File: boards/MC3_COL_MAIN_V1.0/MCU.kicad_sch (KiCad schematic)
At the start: 17 parts, among them J2 SWD, SW1 SKRKAEE020, U2 STM32F411RET6, Y1 8MHz

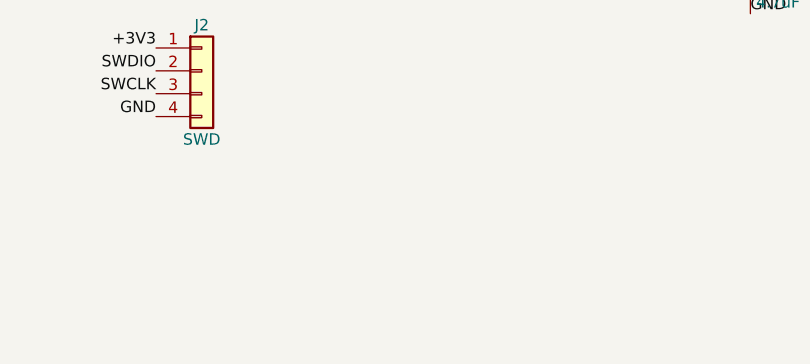
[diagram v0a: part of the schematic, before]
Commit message: Schematic: I2C1 pull-ups (R12/R13 4.7k, PROVISIONAL); DRV8214 layout note; parts README and MIGRATION updated
Co-Authored-By: Claude Fable 5 <noreply@anthropic.com>
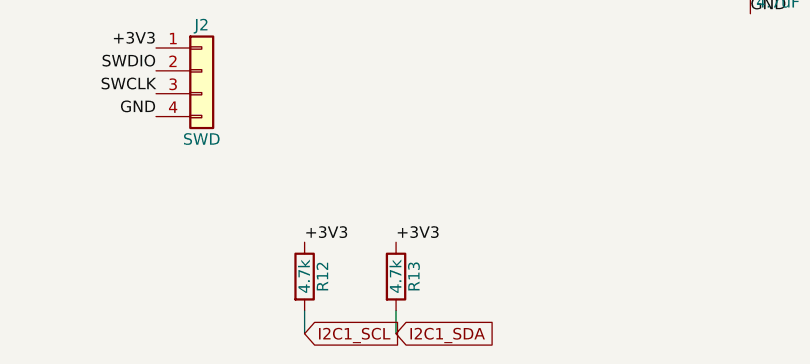
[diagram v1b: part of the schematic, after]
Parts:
- added R12, R13: 4.7k, MC3_COL_MAIN:R_0402_1005Metric, symbol Device:R
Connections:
- net +3V3: now also R12.1, R13.1
- net I2C1_SCL: now also R12.2
- net I2C1_SDA: now also R13.2

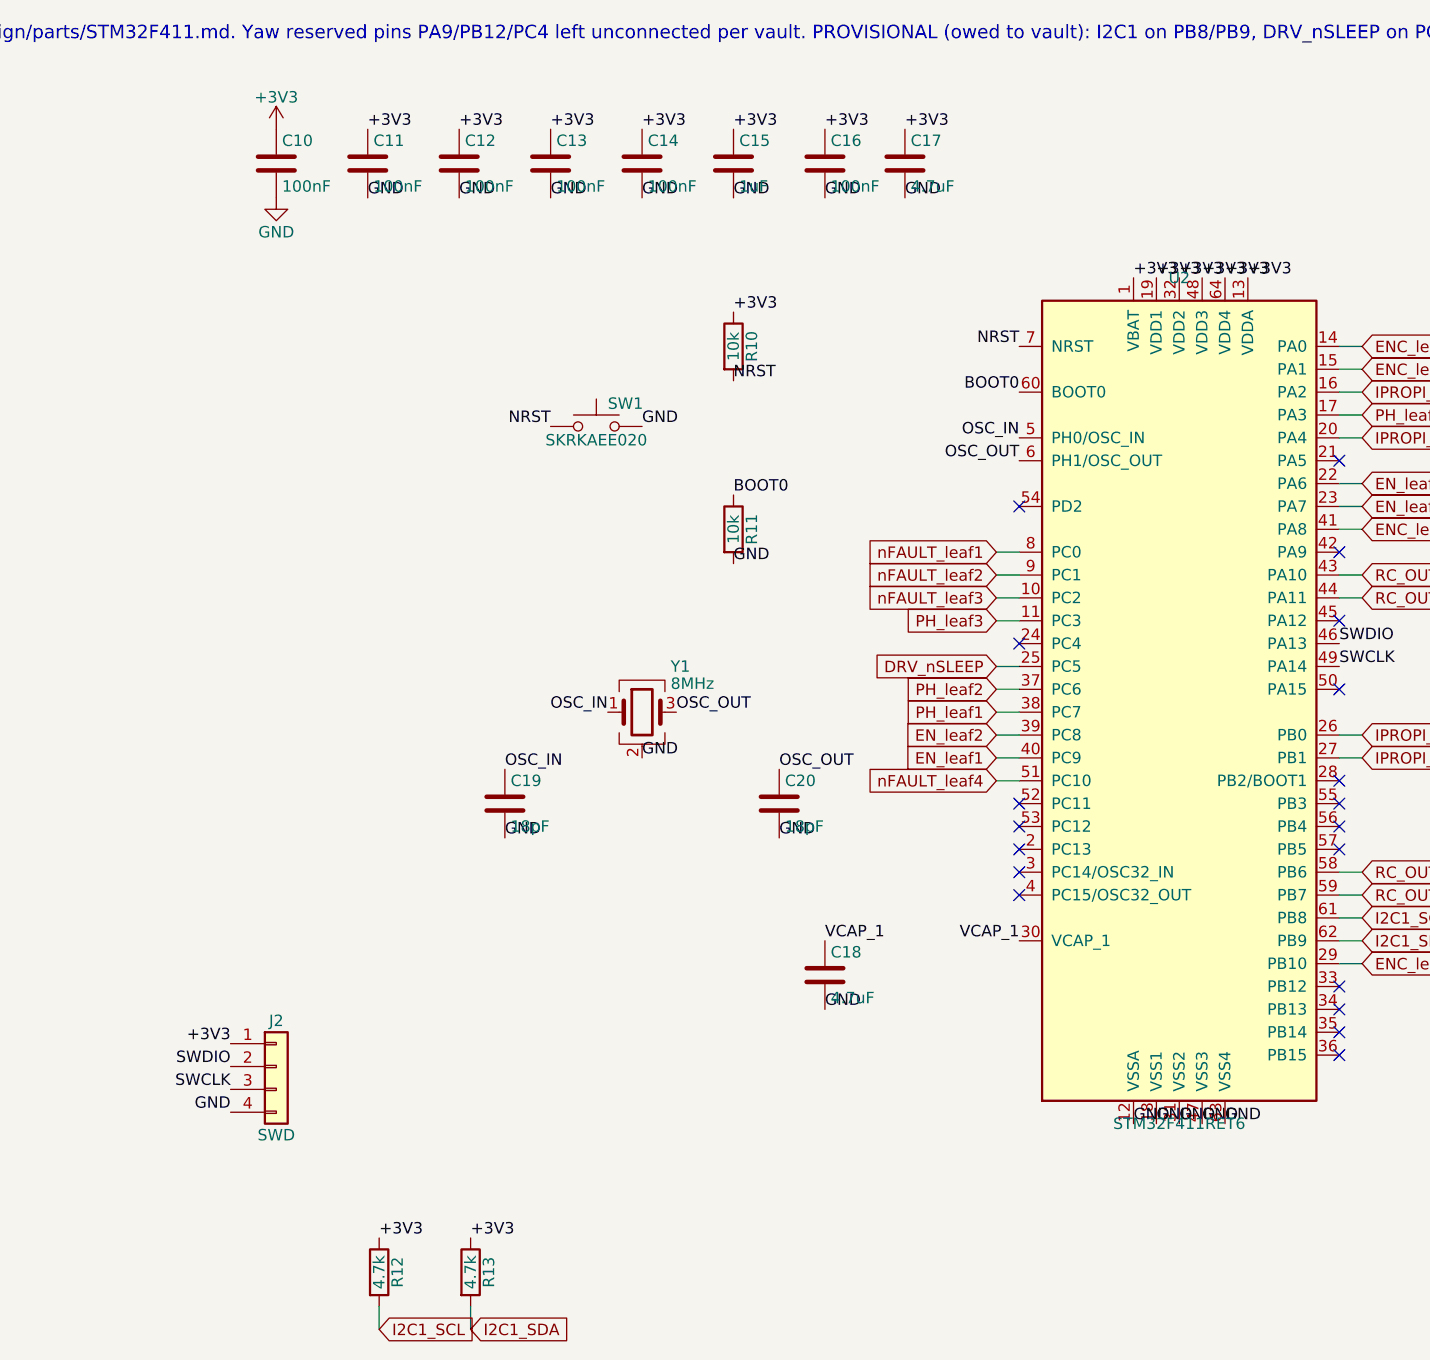
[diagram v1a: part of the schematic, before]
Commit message: Schematic annotated in eeschema (per-instance references for the 4 channel sheets); user review OK
Co-Authored-By: Claude Fable 5 <noreply@anthropic.com>
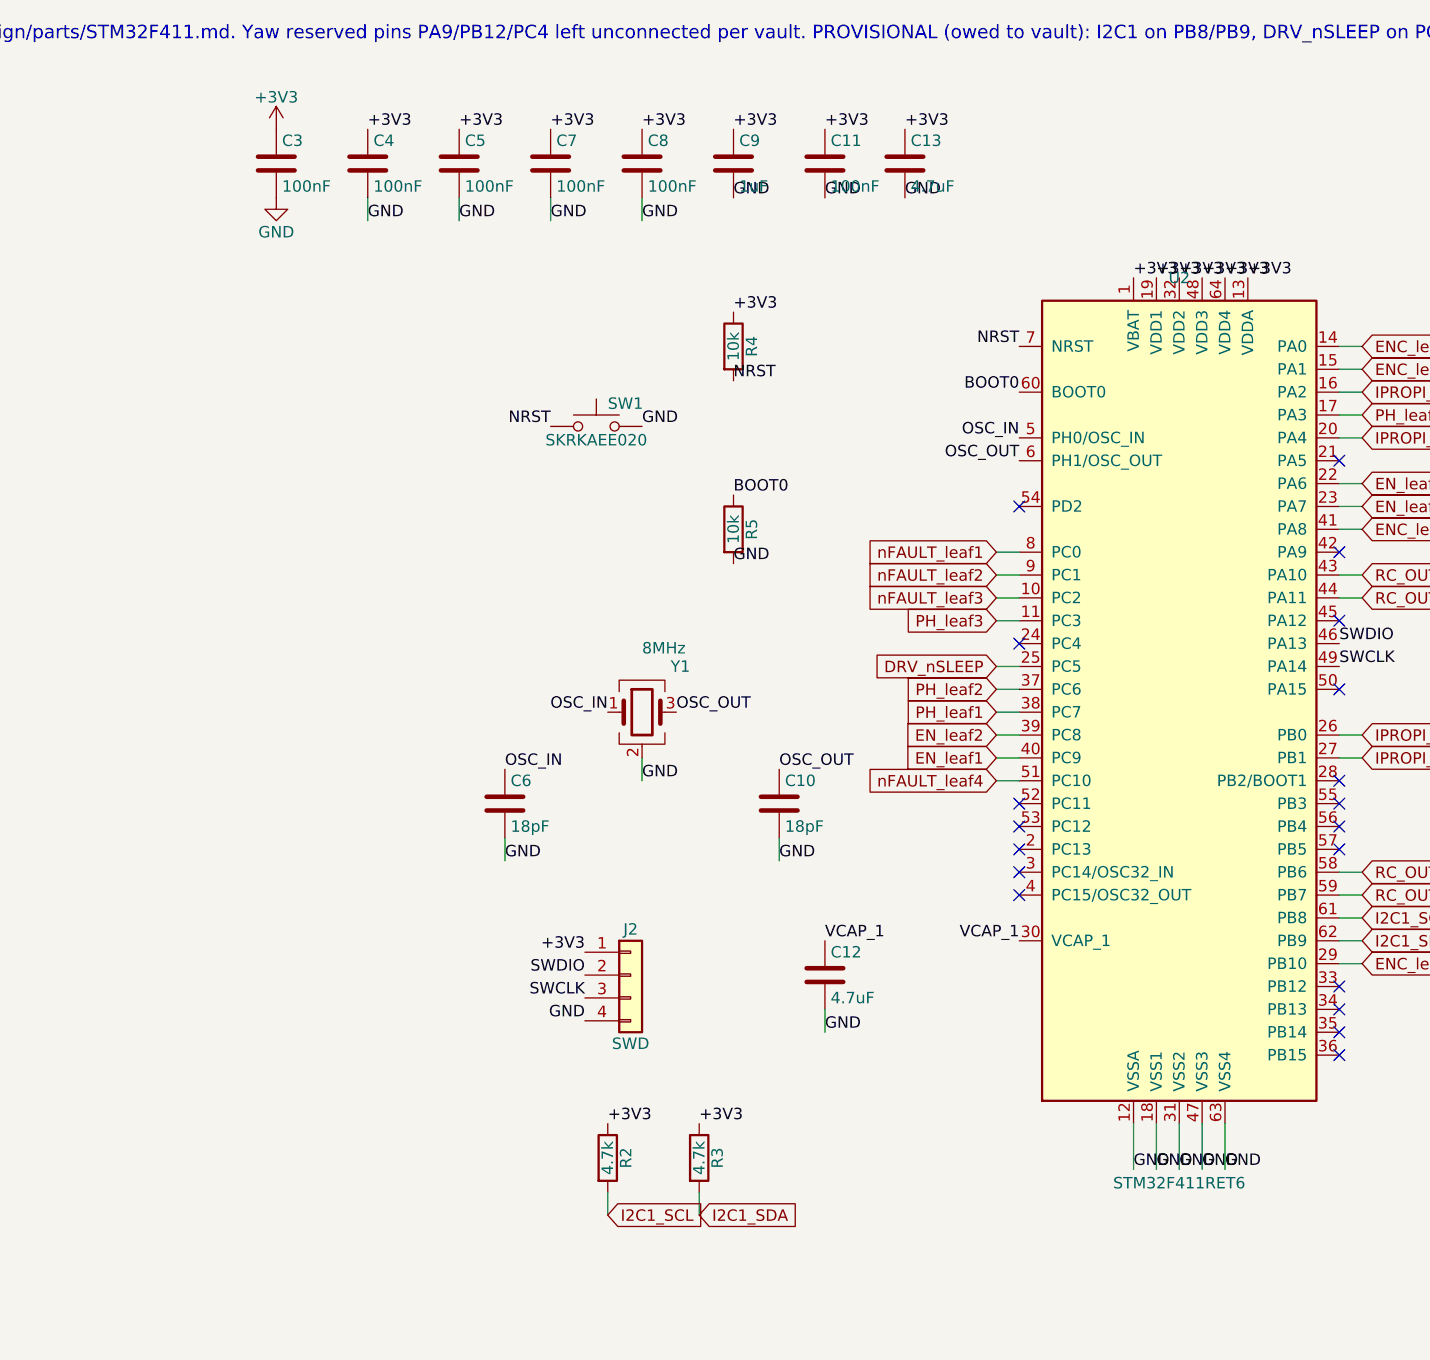
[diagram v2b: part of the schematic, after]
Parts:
- renumbered C20 to C10, C16 to C11, C18 to C12, C17 to C13, C10 to C3, C11 to C4, C12 to C5, C19 to C6, C13 to C7, C14 to C8, C15 to C9, R12 to R2, R13 to R3, R10 to R4, R11 to R5
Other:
- moved on the sheet: J2, R2, R3

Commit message: Remove tscircuit entirely: sources, imports, skills, Node tooling, snapshots; KiCad is the only design tool
Deleted: boards/MC3_COL_MAIN_V1.0/*.tsx|*.ts|tests/, imports/, scripts/, index/postest
.circuit.tsx, manual-edits.json, tscircuit.config.json, tsconfig.json, package.json, bun.lock,
.npmrc, __snapshots__/, .claude/skills/tscircuit/, .agents/skills/tscircuit/ (plus untracked
node_modules/, .tscircuit/, dist/). .gitignore reduced to KiCad/Konnect/IDE entries.
CLAUDE.md banner replaced by a history note; docs/design/parts/STM32F411.md rewritten for the
KiCad schematic.

Co-Authored-By: Claude Fable 5 <noreply@anthropic.com>
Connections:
- net IPROPI_yaw: now reaches U2.24 (PC4)
- net PH_yaw: now reaches U2.33 (PB12)
- net RC_OUT_yaw: now reaches U2.34 (PB13)
- net EN_yaw: now reaches U2.42 (PA9)
- net nFAULT_yaw: now reaches U2.53 (PC12)
- no-connect marks 19 -> 14
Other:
- note added: "2026-08-22: yaw channel FITTED (user decision, supersedes the 'reserved only' note above): EN_yaw PA9 (TIM1_CH2), PH_yaw PB12, IPROPI_yaw PC4 (ADC1_IN14) per vault; PROVISIONAL nFAULT_yaw PC12, RC_OUT_yaw PB13 (EXTI only - no free capture channel; use I2C RC_CNT or EXTI)."

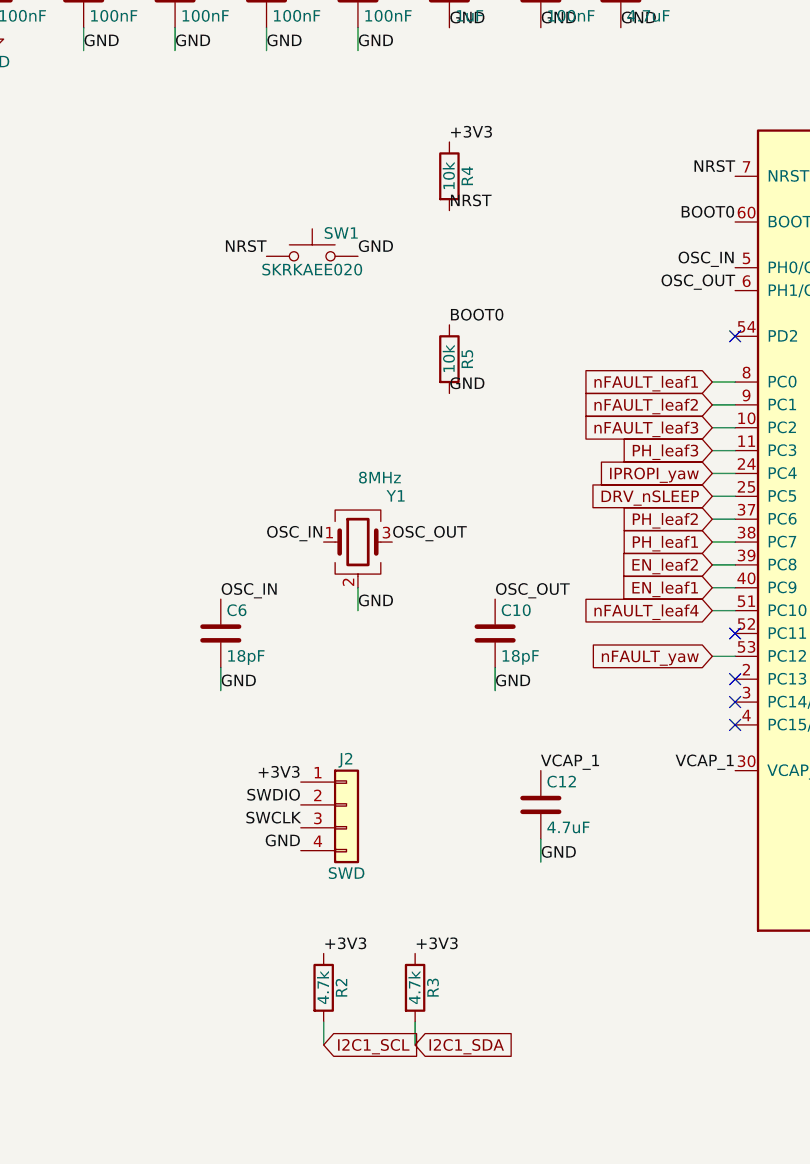
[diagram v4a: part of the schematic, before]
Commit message: Schematic re-annotated in eeschema after yaw channel + strap pull-ups
Co-Authored-By: Claude Fable 5 <noreply@anthropic.com>
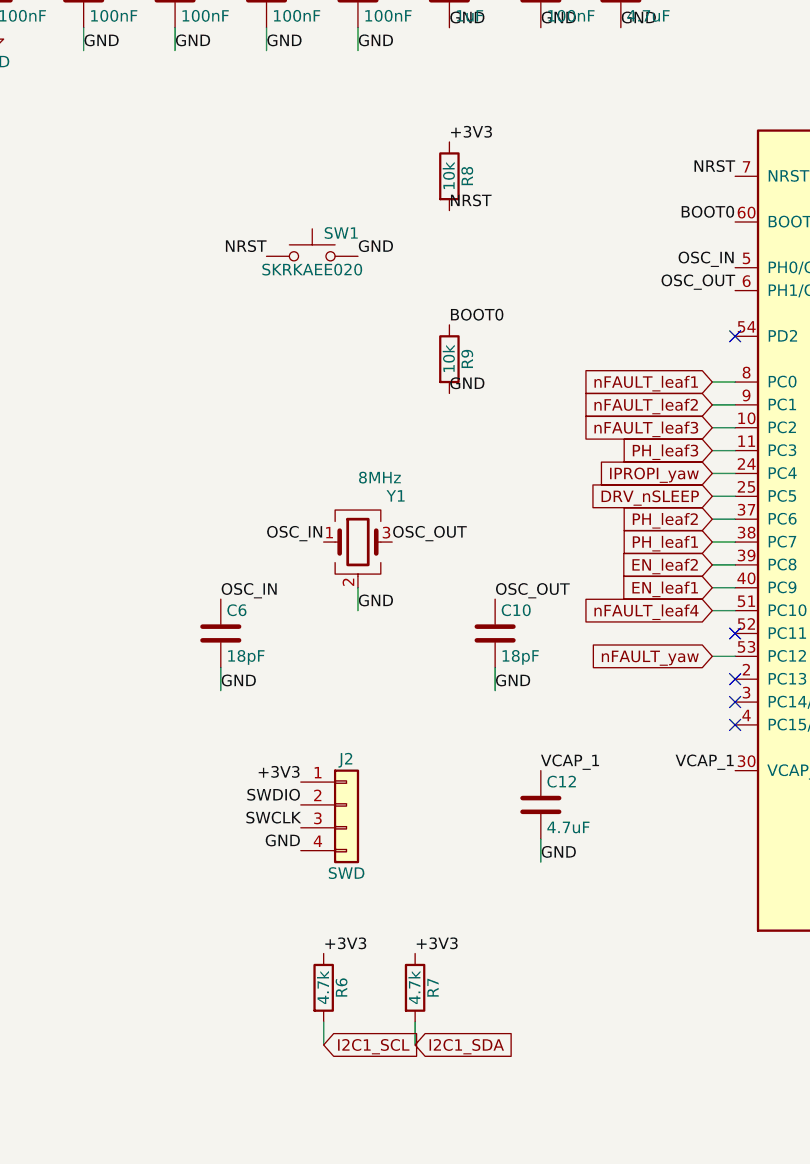
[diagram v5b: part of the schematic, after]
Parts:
- renumbered R2 to R6, R3 to R7, R4 to R8, R5 to R9
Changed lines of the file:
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@@
 		(in_pos_files yes)
 		(dnp no)
-		(property "Reference" "R2"
+		(property "Reference" "R6"
 			(at 88.392 149.86 90)
 			(show_name no)
@@
 			(project "MC3_COL_MAIN_V1.0"
 				(path "/7d5f4202-d55e-4c7b-a2df-dd599db38e48/82019890-1ee3-4edd-b219-f0a654758d61"
-					(reference "R2")
+					(reference "R6")
 					(unit 1)
 				)
@@
 		(in_pos_files yes)
 		(dnp no)
-		(property "Reference" "R5"
+		(property "Reference" "R9"
 			(at 102.362 80.01 90)
 			(show_name no)
@@
 			(project "MC3_COL_MAIN_V1.0"
 				(path "/7d5f4202-d55e-4c7b-a2df-dd599db38e48/82019890-1ee3-4edd-b219-f0a654758d61"
-					(reference "R5")
+					(reference "R9")
 					(unit 1)
 				)
@@
 		(in_pos_files yes)
 		(dnp no)
-		(property "Reference" "R3"
+		(property "Reference" "R7"
 			(at 98.552 149.86 90)
 			(show_name no)
@@
 			(project "MC3_COL_MAIN_V1.0"
 				(path "/7d5f4202-d55e-4c7b-a2df-dd599db38e48/82019890-1ee3-4edd-b219-f0a654758d61"
-					(reference "R3")
+					(reference "R7")
 					(unit 1)
 				)
@@
 		(in_pos_files yes)
 		(dnp no)
-		(property "Reference" "R4"
+		(property "Reference" "R8"
 			(at 102.362 59.69 90)
 			(show_name no)
@@
 			(project "MC3_COL_MAIN_V1.0"
 				(path "/7d5f4202-d55e-4c7b-a2df-dd599db38e48/82019890-1ee3-4edd-b219-f0a654758d61"
-					(reference "R4")
-					(unit 1)
-				)
+					(reference "R8")
+					(unit 1)
+				)
